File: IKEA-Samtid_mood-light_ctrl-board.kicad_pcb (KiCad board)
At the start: 2 copper layers, 41.3 x 15.5 mm, 16 parts, among them IC1 ATMEGA168PA-M, P1 FTDI, P3.2 B-to-B-1B, P4.2 B-to-B-2B, SW1 ENTER, SW2 MODE, X1 CSTCE16M0V53-R0

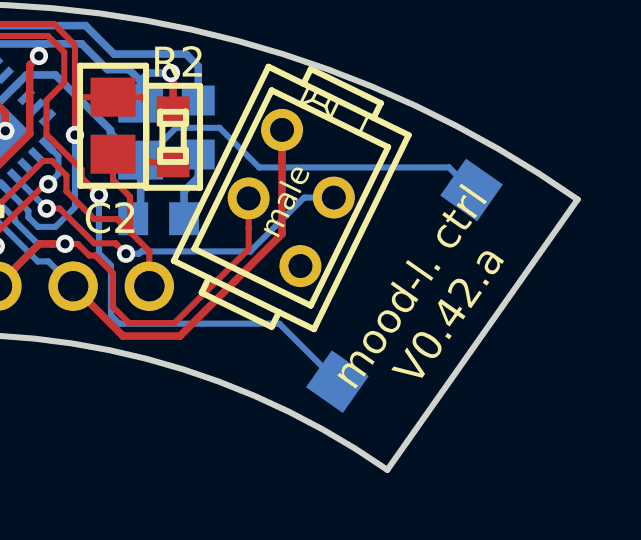
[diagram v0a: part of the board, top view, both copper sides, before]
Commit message: Playing with mini-T power connector. Feasibility test.
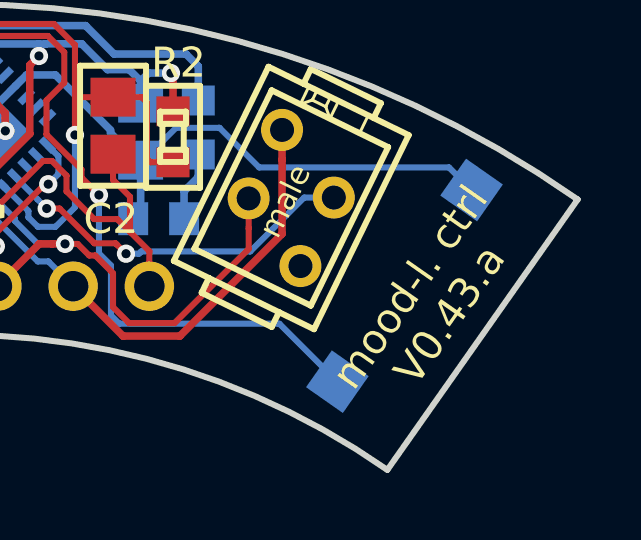
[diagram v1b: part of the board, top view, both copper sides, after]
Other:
- board text added: "mood-l. ctrl V0.43.a"
- board text removed: "mood-l. ctrl V0.42.a"
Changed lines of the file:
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@@
     (title IKEA-Samtid_mood-light_ctrl-board)
     (date "Thu 05 Feb 2015")
-    (rev 0.42.a)
+    (rev 0.43.a)
     (company "2015 - blog.spitzenpfeil.org")
   )
@@
     (effects (font (size 1 1) (thickness 0.2)))
   )
-  (gr_text "mood-l. ctrl\nV0.42.a" (at 165.83 97.13 55) (layer F.SilkS)
+  (gr_text "mood-l. ctrl\nV0.43.a" (at 165.83 97.13 55) (layer F.SilkS)
     (effects (font (size 1 1) (thickness 0.2)))
   )

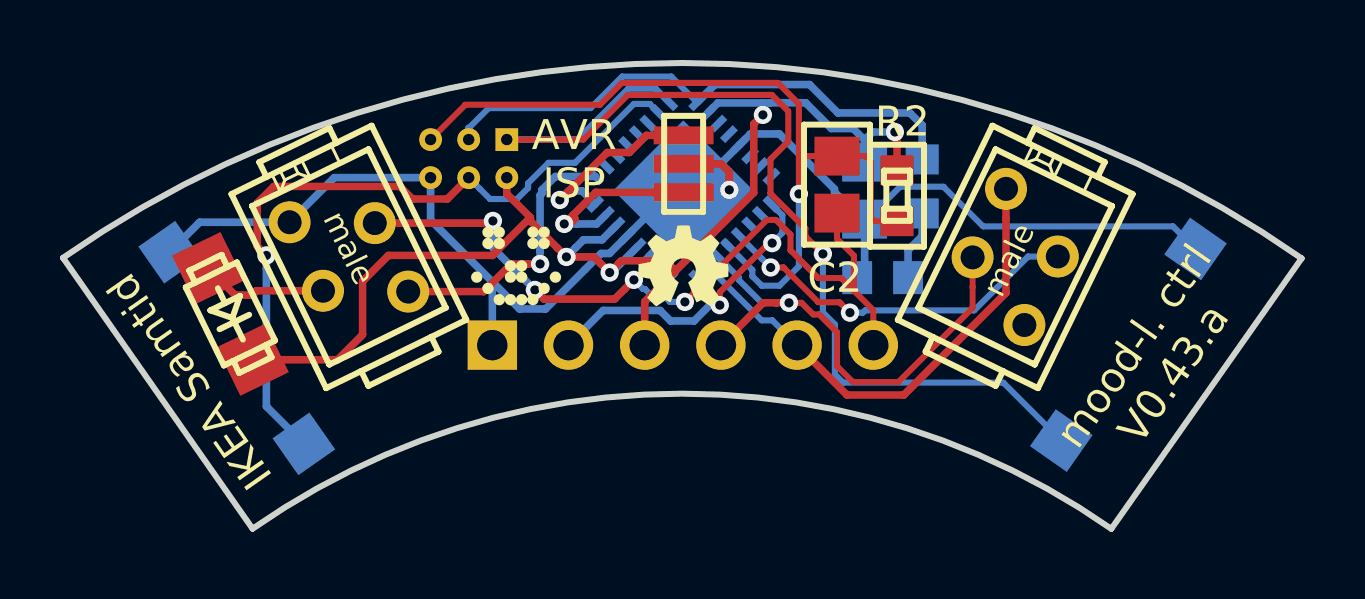
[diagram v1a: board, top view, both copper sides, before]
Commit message: Ctrl-board tweaks.
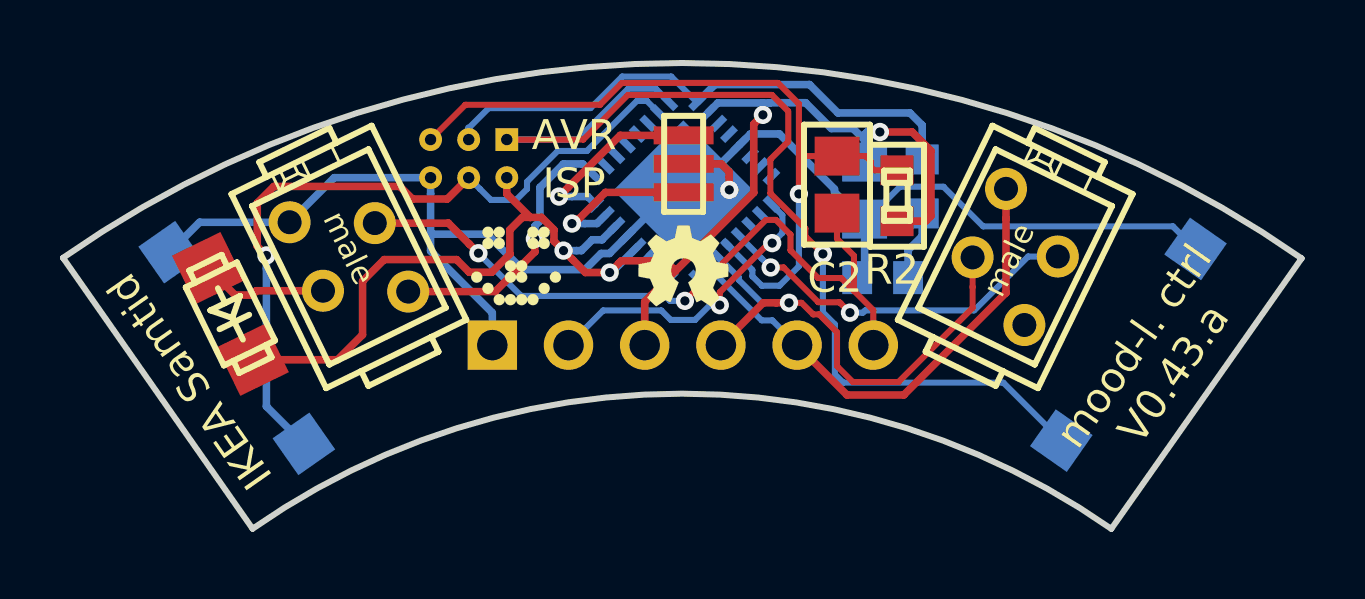
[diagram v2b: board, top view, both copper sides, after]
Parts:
- turned R2 to 90 degrees
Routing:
- net /VCC.B2: track 42.1 -> 46.7 mm
- net /RST: track 27.5 -> 25.8 mm
- net /GND.B: track 53.5 -> 55.1 mm
- net /DTR.B: track 26.1 -> 24.9 mm, vias 4 -> 2
- net /XTAL1: track 6.39 -> 5.52 mm

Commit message: Rerouted the ctrl-board.
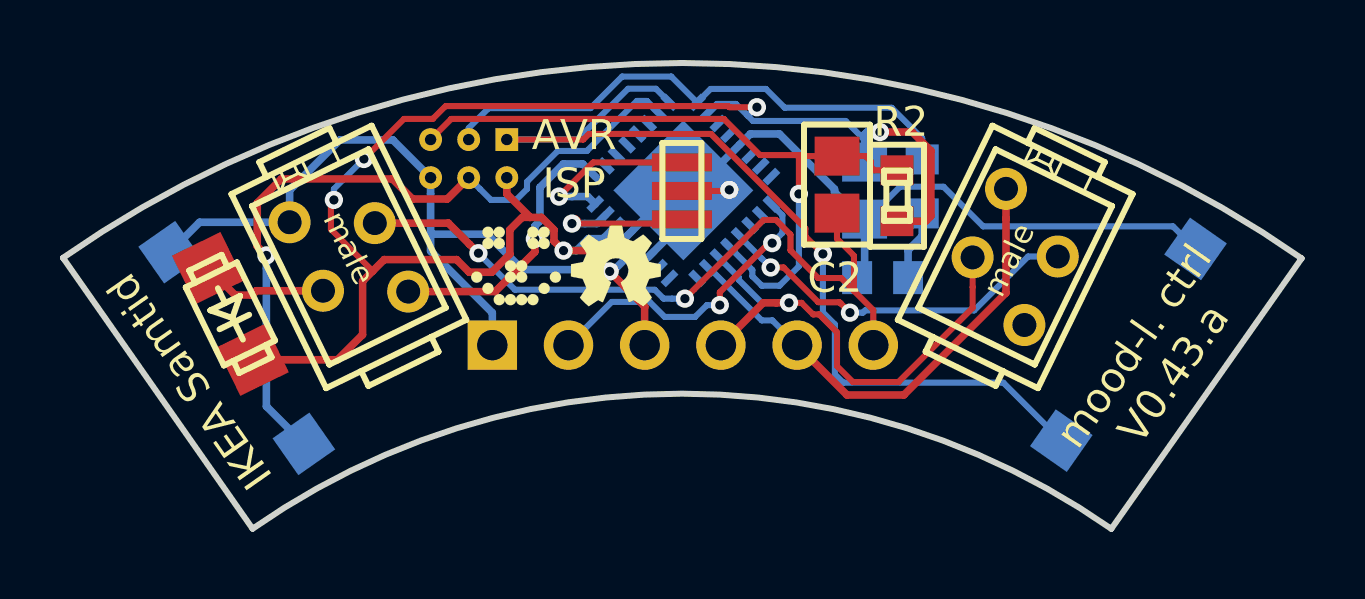
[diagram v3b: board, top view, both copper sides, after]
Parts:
- moved LOGO2 2.25 mm to (147.9, 94.0)
- moved X1 0.90 mm to (150.1, 91.5)
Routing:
- net /VCC.B2: track 46.7 -> 56.4 mm, vias 4 -> 6
- net /MISO: track 34.9 -> 31.4 mm
- net /RST: track 25.8 -> 23.8 mm
- net /GND.B: track 55.1 -> 56.2 mm

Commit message: Moved DS1 from ctrl-board to main board (before 3.3V reg)
--> correct pull-up voltage on level-shifter (== VCC of micro).
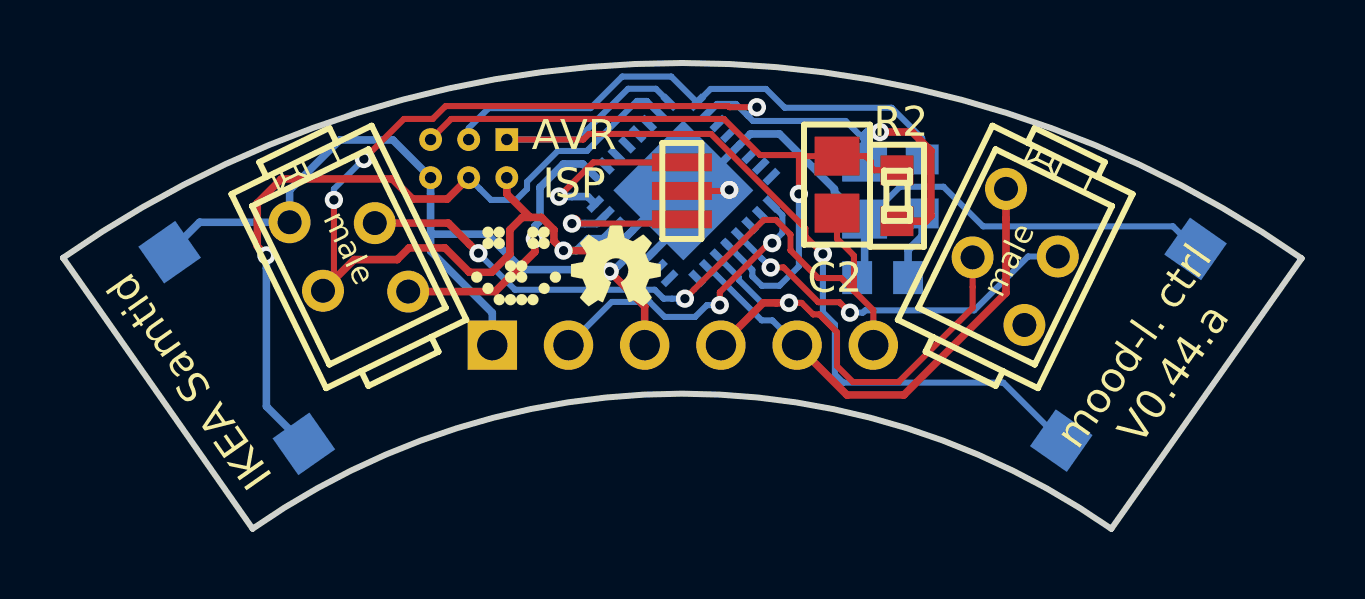
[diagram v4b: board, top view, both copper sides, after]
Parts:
- removed DS1: SS14L, my_parts:MADW__diode_sub-SMA
- C2: value 1nF -> 1nF-ish
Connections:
- C1 pad 1: /VCC.B2 -> /VCC.B
- IC1 pad 18: /VCC.B2 -> /VCC.B
- IC1 pad 4: /VCC.B2 -> /VCC.B
- IC1 pad 6: /VCC.B2 -> /VCC.B
- JP1 pad 2: /VCC.B2 -> /VCC.B
- P1 pad 3: /VCC.B2 -> /VCC.B
- R2 pad 1: /VCC.B2 -> /VCC.B
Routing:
- net /VCC.B2: track 56.4 -> 0.00 mm, vias 6 -> 0
- net /VCC.B: track 4.26 -> 52.7 mm, vias 0 -> 6
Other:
- board text added: "mood-l. ctrl V0.44.a"
- board text removed: "mood-l. ctrl V0.43.a"
